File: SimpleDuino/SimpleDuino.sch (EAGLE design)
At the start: 16 parts, among them J2 POWER_JACKPOWER_JACK_SMD, U1 V_REG_LD1117, U2 ATMEGA328P-PU, Y1 ABL-16.000MHZ-B4Y

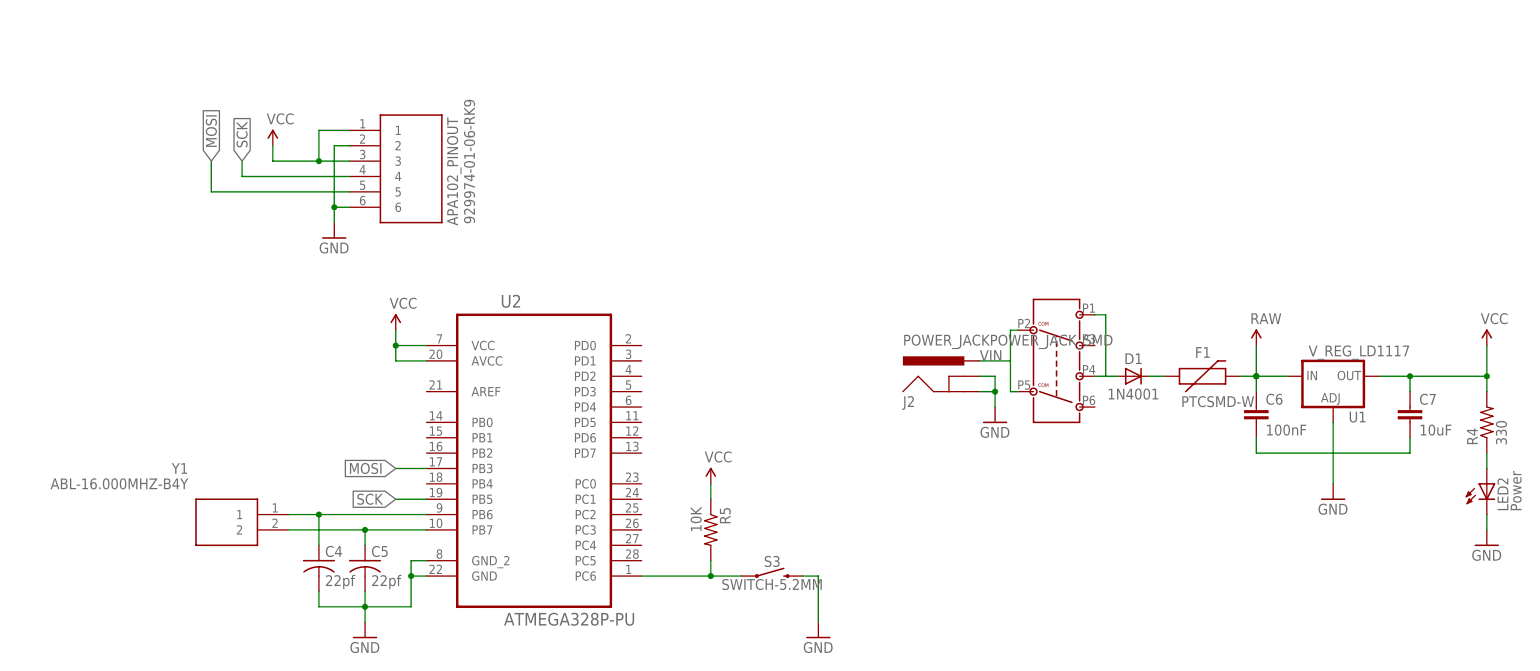
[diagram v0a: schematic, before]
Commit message: Added additional headers and restructured pcb layout.
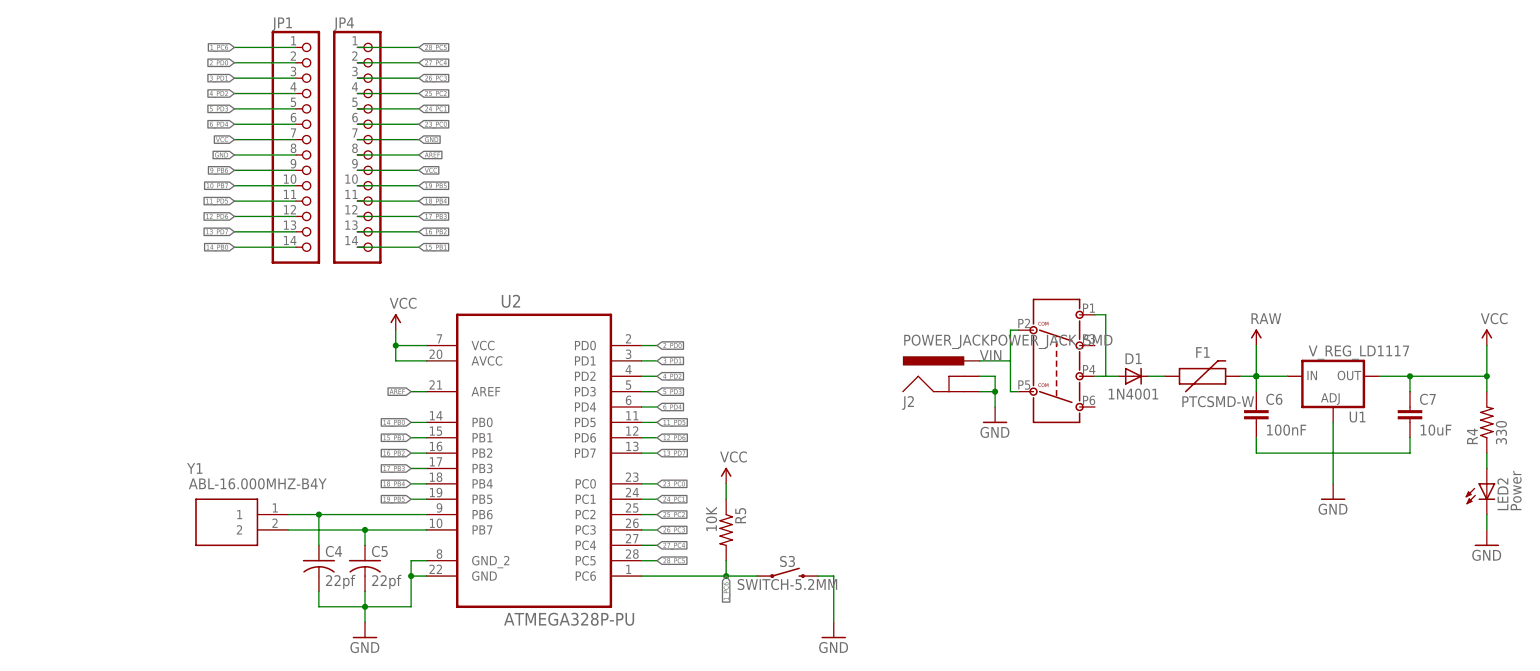
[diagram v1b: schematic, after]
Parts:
- removed APA102_PINOUT: 929974-01-06-RK9, SamacSys_Parts:929974-01-06-RK929974-01-06-RK
- added JP1, JP4: (no value), pinhead:PINHD-1X14
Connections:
- removed net MOSI: APA102_PINOUT.5, U2.PB3
- removed net N$3: C4.1, U2.PB6, Y1.1
- removed net N$6: C5.1, U2.PB7, Y1.2
- removed net N$7: R5.2, S3.1, U2.PC6
- removed net SCK: APA102_PINOUT.4, U2.PB5
- new net 10_PB7: C5.1, JP1.10, U2.PB7, Y1.2
- new net 11_PD5: JP1.11, U2.PD5
- new net 12_PD6: JP1.12, U2.PD6
- new net 13_PD7: JP1.13, U2.PD7
- new net 14_PB0: JP1.14, U2.PB0
- new net 15_PB1: JP4.14, U2.PB1
- new net 16_PB2: JP4.13, U2.PB2
- new net 17_PB3: JP4.12, U2.PB3
- new net 18_PB4: JP4.11, U2.PB4
- new net 19_PB5: JP4.10, U2.PB5
- new net 1_PC6: JP1.1, R5.2, S3.1, U2.PC6
- new net 23_PC0: JP4.6, U2.PC0
- new net 24_PC1: JP4.5, U2.PC1
- new net 25_PC2: JP4.4, U2.PC2
- new net 26_PC3: JP4.3, U2.PC3
- new net 27_PC4: JP4.2, U2.PC4
- new net 28_PC5: JP4.1, U2.PC5
- new net 2_PD0: JP1.2, U2.PD0
- new net 3_PD1: JP1.3, U2.PD1
- new net 4_PD2: JP1.4, U2.PD2
- new net 5_PD3: JP1.5, U2.PD3
- new net 6_PD4: JP1.6, U2.PD4
- new net 9_PB6: C4.1, JP1.9, U2.PB6, Y1.1
- new net AREF: JP4.8, U2.AREF
- net GND: now also JP1.8, JP4.7; no longer APA102_PINOUT.2, APA102_PINOUT.6
- net VCC: now also JP1.7, JP4.9; no longer APA102_PINOUT.1, APA102_PINOUT.3
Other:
- moved on the sheet: R5, S3
